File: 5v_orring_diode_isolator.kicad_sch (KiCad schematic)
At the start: 13 parts, among them U3 NID1500, U4 NID1500

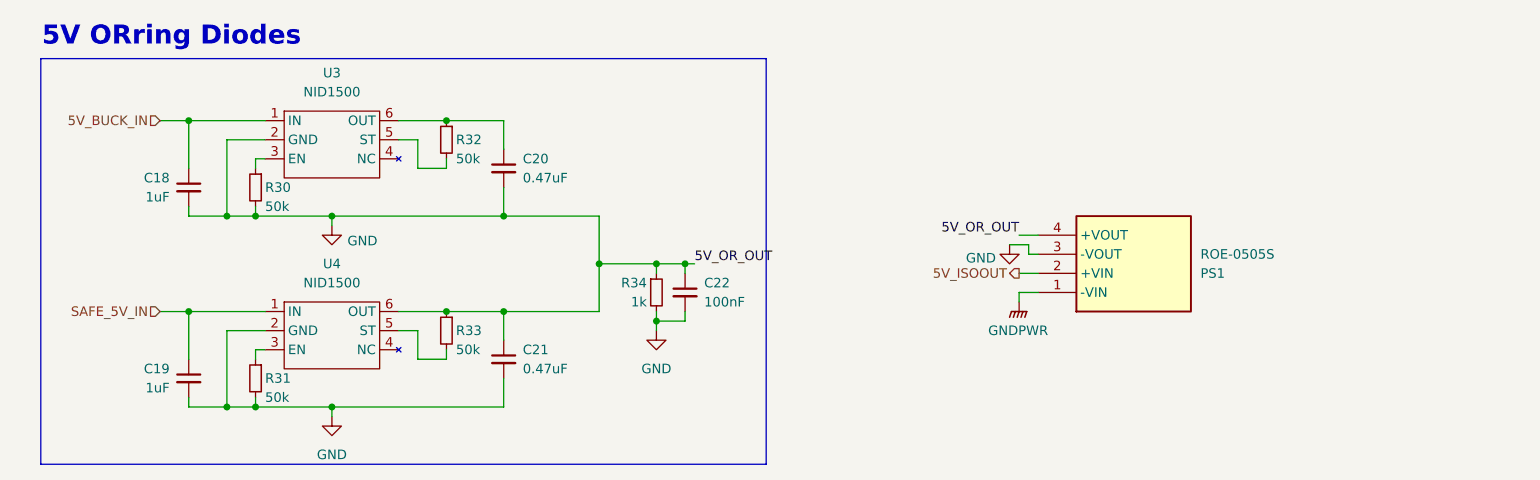
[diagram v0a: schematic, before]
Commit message: cleaned up schematic, added power LEDs and testpoints
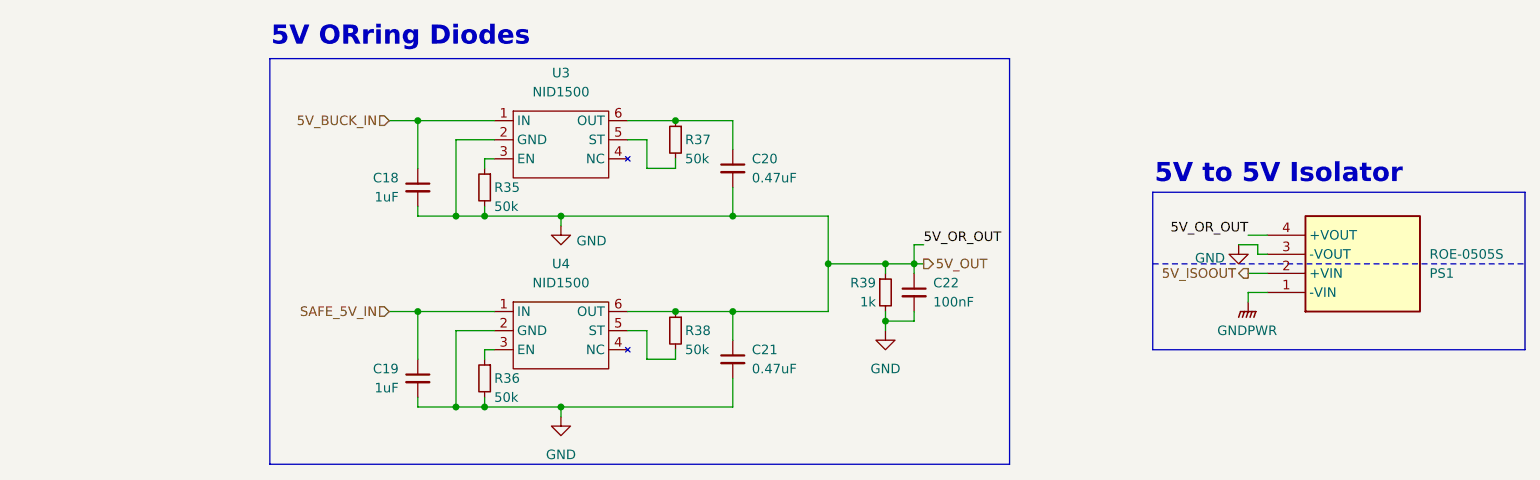
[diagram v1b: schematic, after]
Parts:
- renumbered R30 to R35, R31 to R36, R32 to R37, R33 to R38, R34 to R39
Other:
- note added: "5V to 5V Isolator"
- moved on the sheet: C18, C19, C20, C21, C22, PS1, R35, R36, R37, R38, R39, U3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

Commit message: finished footprint assignment
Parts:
- R35, R36, R37, R38, R39: footprint (none) -> Resistor_SMD:R_0805_2012Metric
- U3, U4: footprint (none) -> Package_TO_SOT_SMD:SOT-363_SC-70-6
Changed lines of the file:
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@@
 			)
 		)
-		(property "Footprint" ""
+		(property "Footprint" "Resistor_SMD:R_0805_2012Metric"
 			(at 90.17 95.25 0)
 			(effects
@@
 			)
 		)
-		(property "Footprint" ""
+		(property "Footprint" "Package_TO_SOT_SMD:SOT-363_SC-70-6"
 			(at 100.33 115.57 0)
 			(effects
@@
 			)
 		)
-		(property "Footprint" ""
+		(property "Footprint" "Resistor_SMD:R_0805_2012Metric"
 			(at 143.51 109.22 0)
 			(effects
@@
 			)
 		)
-		(property "Footprint" ""
+		(property "Footprint" "Resistor_SMD:R_0805_2012Metric"
 			(at 115.57 88.9 0)
 			(effects
@@
 			)
 		)
-		(property "Footprint" ""
+		(property "Footprint" "Package_TO_SOT_SMD:SOT-363_SC-70-6"
 			(at 100.33 90.17 0)
 			(effects
@@
 			)
 		)
-		(property "Footprint" ""
+		(property "Footprint" "Resistor_SMD:R_0805_2012Metric"
 			(at 115.57 114.3 0)
 			(effects
@@
 			)
 		)
-		(property "Footprint" ""
+		(property "Footprint" "Resistor_SMD:R_0805_2012Metric"
 			(at 90.17 120.65 0)
 			(effects

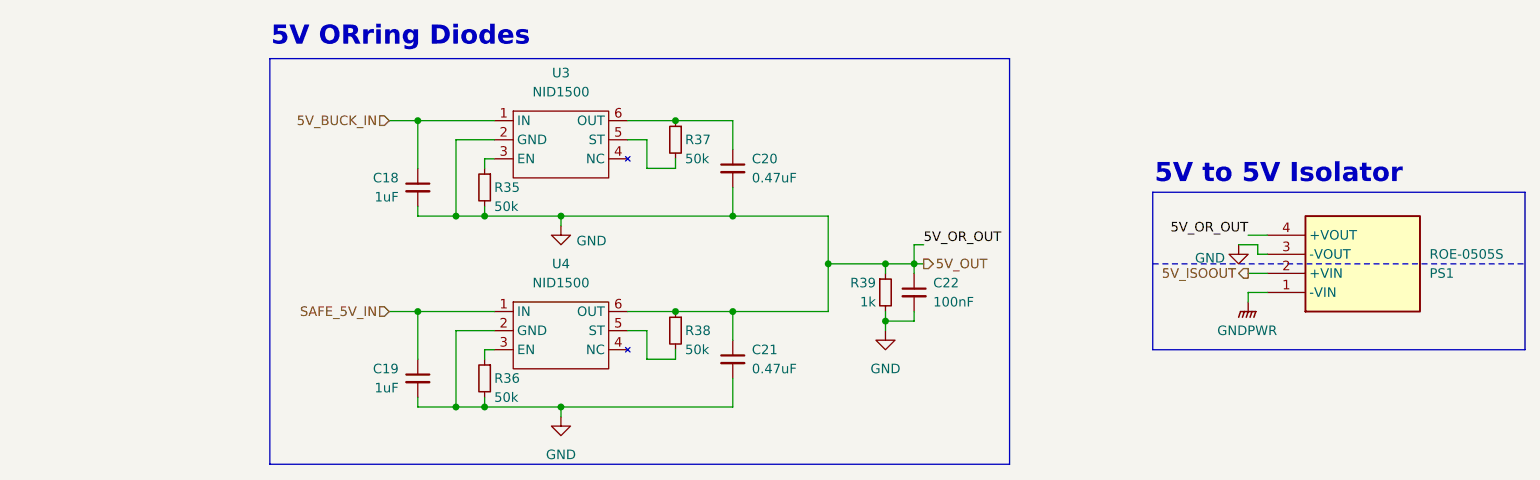
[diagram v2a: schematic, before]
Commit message: address review changes, add more output protections
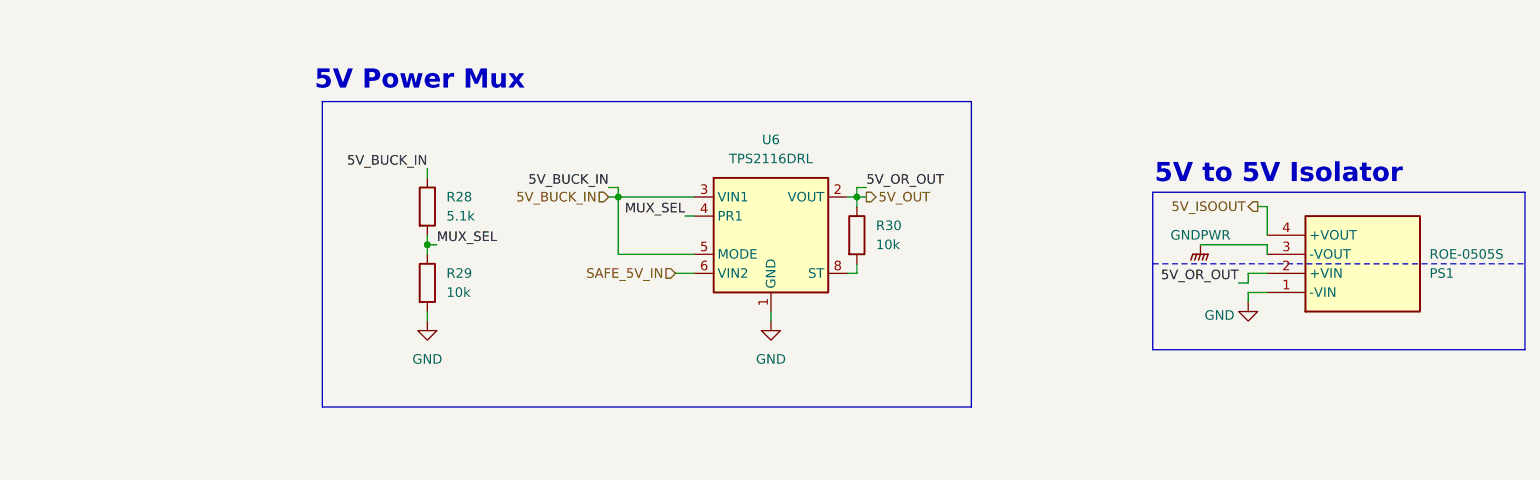
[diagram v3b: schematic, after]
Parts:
- removed C18, C19: 1uF, Capacitor_SMD:C_0805_2012Metric, symbol Device:C_Small
- removed C20, C21: 0.47uF, Capacitor_SMD:C_0805_2012Metric, symbol Device:C_Small
- removed C22: 100nF, Capacitor_SMD:C_0805_2012Metric, symbol Device:C_Small
- removed R35, R36, R37, R38: 50k, Resistor_SMD:R_0805_2012Metric, symbol Device:R_Small
- removed R39: 1k, Resistor_SMD:R_0805_2012Metric, symbol Device:R_Small
- removed U3, U4: NID1500, Package_TO_SOT_SMD:SOT-363_SC-70-6, symbol utsvt-chips:NID1500
- added R28: 5.1k, symbol Device:R
- added R29, R30: 10k, symbol Device:R
- added U6: TPS2116DRL, Package_TO_SOT_SMD:SOT-583-8, symbol Power_Management:TPS2116DRL
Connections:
- net 5V_BUCK_IN: now also R28.1, U6.3 (VIN1), U6.5 (MODE)
- net 5V_ISOOUT: now also PS1.4 (+VOUT); no longer PS1.2 (+VIN)
- net GND: now also PS1.1 (-VIN), R29.2, U6.1 (GND); no longer PS1.3 (-VOUT), PS1.4 (+VOUT)
- net GNDPWR: now also PS1.3 (-VOUT); no longer PS1.1 (-VIN)
- net SAFE_5V_IN: now also U6.6 (VIN2)
- new net: R30.2, U6.8 (ST)
- new net 5V_OUT: PS1.2 (+VIN), R30.1, U6.2 (VOUT), U6.7 (VOUT)
- new net MUX_SEL: R28.2, R29.1, U6.4 (PR1)
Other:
- note added: "5V Power Mux"
- note removed: "5V ORring Diodes"
